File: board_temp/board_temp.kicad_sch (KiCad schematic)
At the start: 16 parts, among them J1 Conn_02x16_Odd_Even, J2 Battery input, J3 USB_C_Receptacle_PowerOnly_6P, SW1 SW_SP3T, U1 BQ24074RGT, U2 INA219AxDCN, U3 IP2721

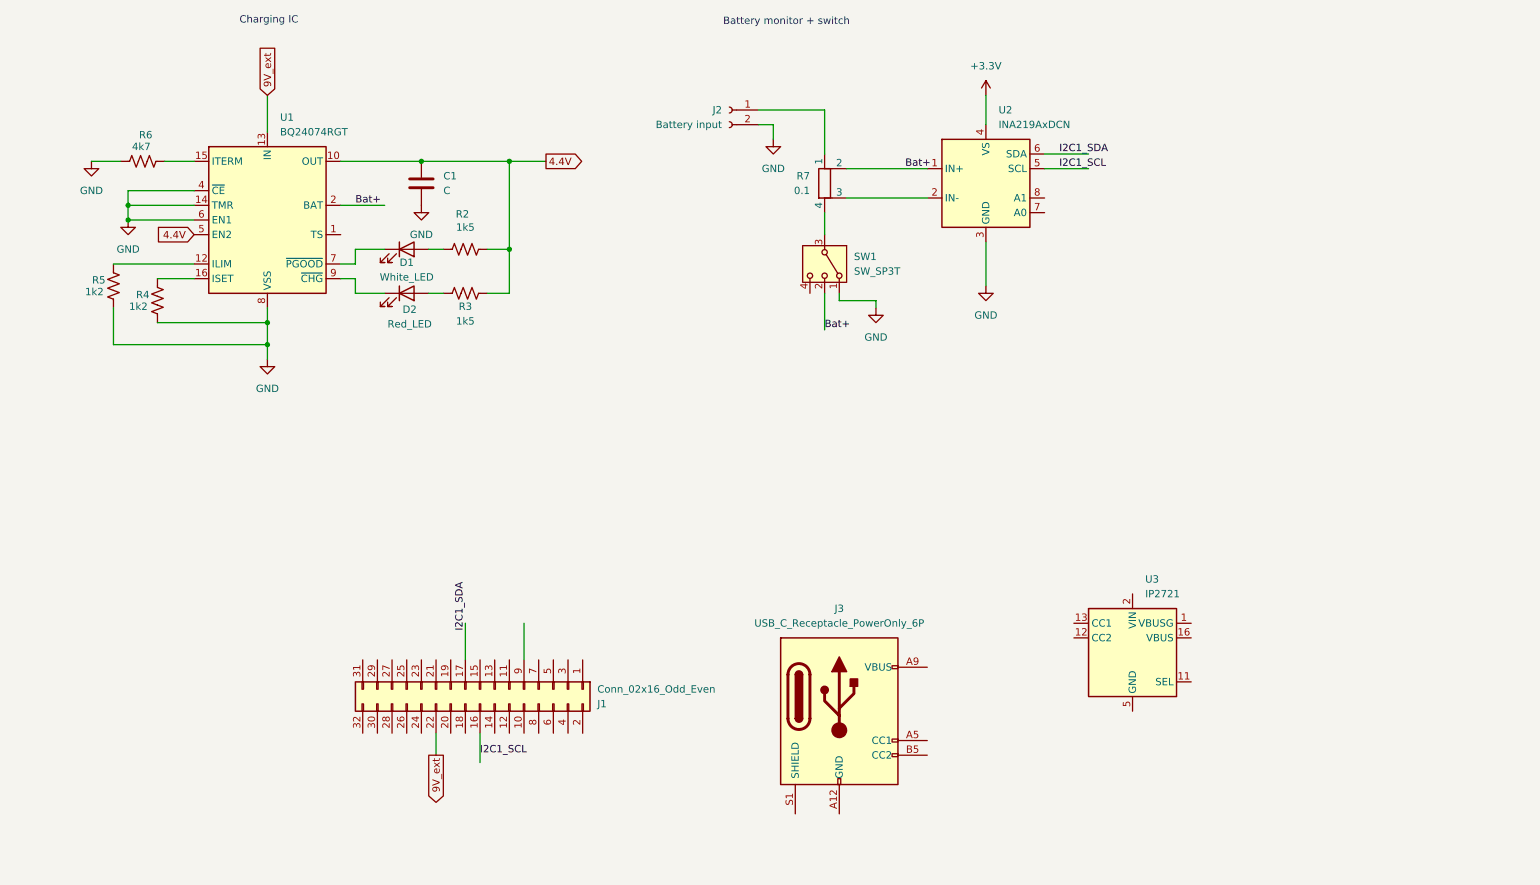
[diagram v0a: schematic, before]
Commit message: changed charging config
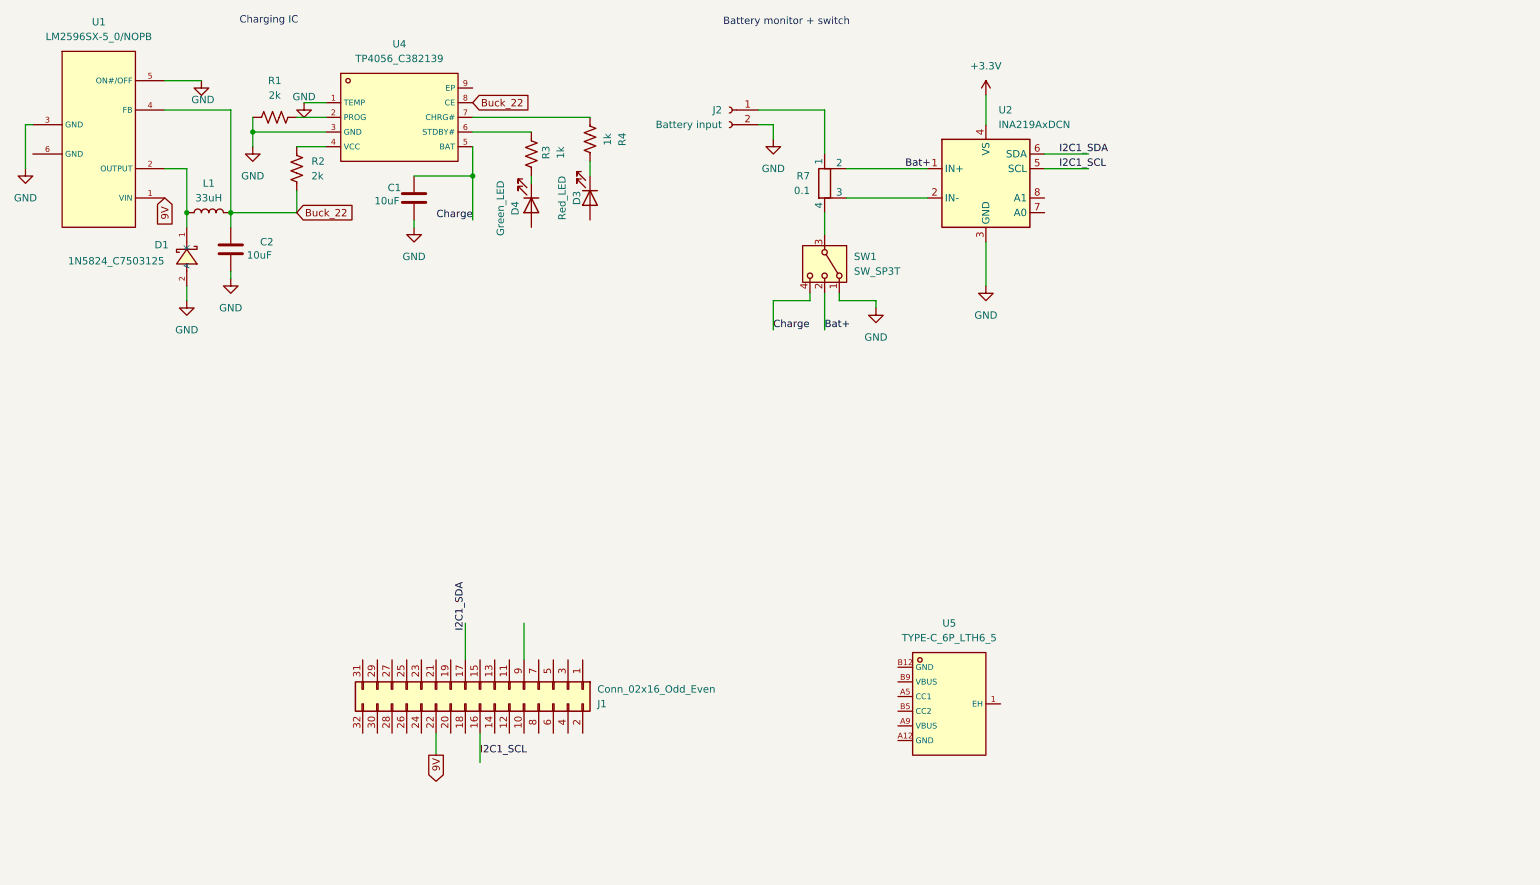
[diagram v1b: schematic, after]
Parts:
- removed D1: White_LED, symbol Device:LED
- removed D2: Red_LED, symbol Device:LED
- removed J3: USB_C_Receptacle_PowerOnly_6P, symbol Connector:USB_C_Receptacle_PowerOnly_6P
- removed R5: 1k2, symbol Device:R_US
- removed R6: 4k7, symbol Device:R_US
- removed U1: BQ24074RGT, Package_DFN_QFN:VQFN-16-1EP_3x3mm_P0.5mm_EP1.6x1.6mm, symbol Battery_Management:BQ24074RGT
- removed U3: IP2721, Package_SO:TSSOP-16_4.4x5mm_P0.65mm, symbol Interface_USB:IP2721
- added C2: 10uF, symbol Device:C
- added D1: 1N5824_C7503125, xxcustom_footprint:DO-27_BD5.3-L8.4-P12.40-D1.3-RD, symbol 1N5824_C7503125:1N5824_C7503125
- added D3: Red_LED, symbol Device:LED
- added D4: Green_LED, symbol Device:LED
- added L1: 33uH, symbol Device:L
- added R1: 2k, xxcustom_footprint:R0402, symbol Device:R_US
- added U1: LM2596SX-5_0/NOPB, xxcustom_footprint:TO-263-5_L10.2-W8.9-P1.70-TL, symbol LM2596SX-5_0/NOPB:LM2596SX-5_0/NOPB
- added U4: TP4056_C382139, xxcustom_footprint:ESOP-8_L4.9-W3.9-P1.27-LS6.0-BL-EP, symbol TP4056_C382139:TP4056_C382139
- added U5: TYPE-C_6P_LTH6_5, xxcustom_footprint:USB-TYPE-C-SMD_TYPE-C-6P-LTH6.5, symbol TYPE-C_6P_LTH6_5:TYPE-C_6P_LTH6_5
- C1: value C -> 10uF
- R2: value 1k5 -> 2k; footprint (none) -> xxcustom_footprint:R0402
- R3: value 1k5 -> 1k; footprint (none) -> xxcustom_footprint:R0402
- R4: value 1k2 -> 1k; footprint (none) -> xxcustom_footprint:R0402
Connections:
- net GND: now also C2.2, D1.2 (A), R1.1, U1.3 (GND), U1.5 (ON#/OFF), U4.1 (TEMP), U4.3 (GND); no longer R4.1
- net at R4.2: now also U4.7 (CHRG#)
- net Charge: now reaches SW1.4
- net Charge: now also C1.1, U4.5 (BAT)
- net at R3.1: now also U4.6 (STDBY#)
- net Buck_22: now reaches R2.1
- net Buck_22: now also C2.1, L1.2, U1.4 (FB), U4.8 (CE)
- removed net 4.4V: C1.1, R2.2, R3.2
- net 9V_ext renamed 9V
- net 9V: now also U1.1 (VIN)
- new net: D3.1 (K), R4.1
- new net: D1.1 (K), L1.1, U1.2 (OUTPUT)
- new net: D4.1 (K), R3.2
- new net: R1.2, U4.2 (PROG)
- new net: R2.2, U4.4 (VCC)

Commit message: reorganized some files
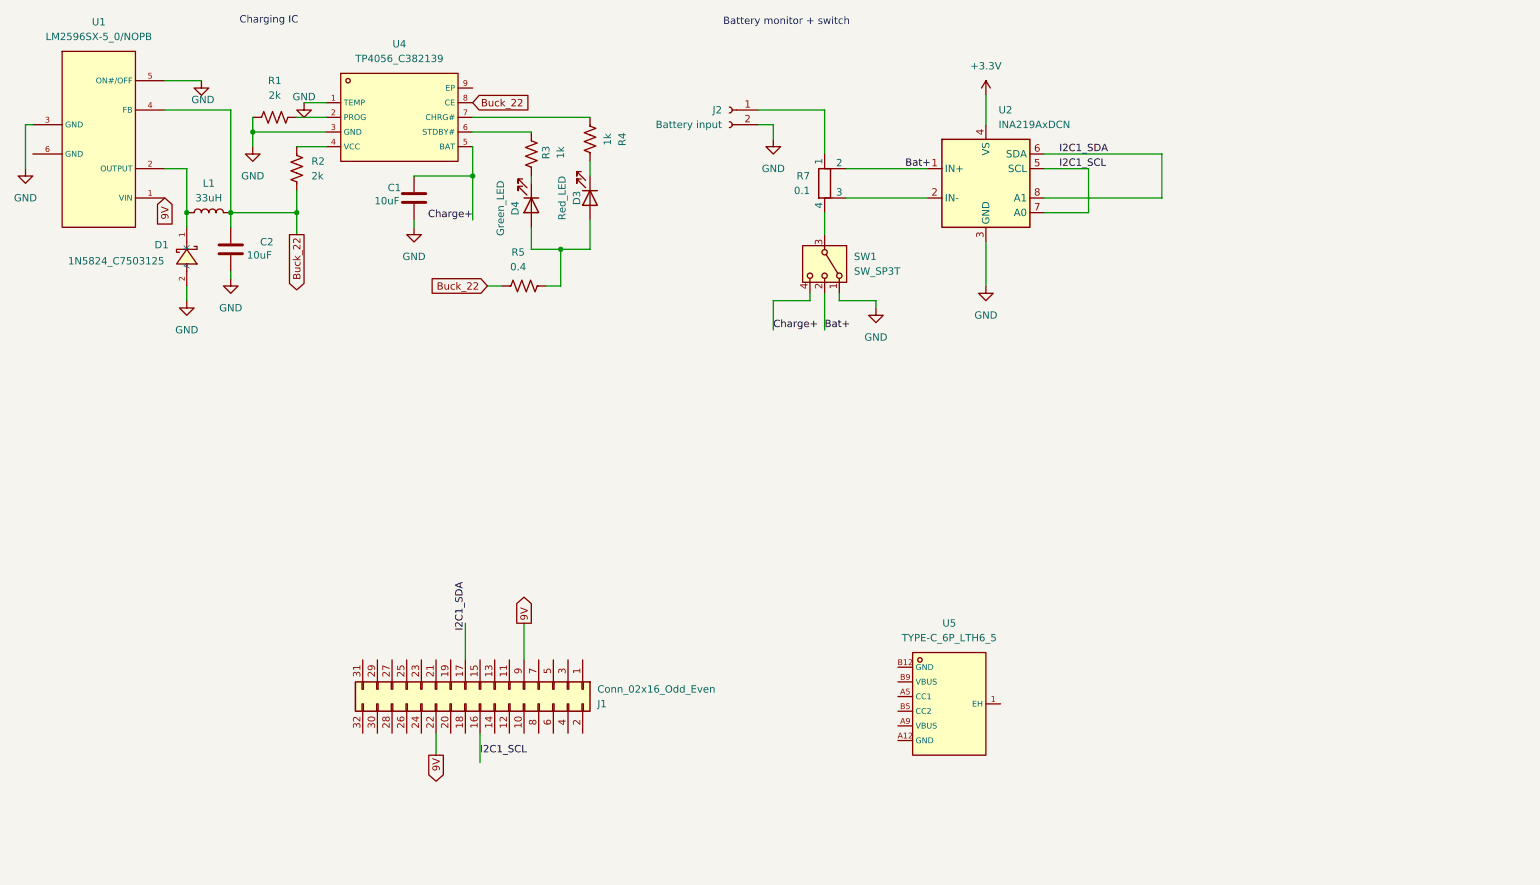
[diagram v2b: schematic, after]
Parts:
- added R5: 0.4, symbol Device:R_US
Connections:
- net 9V: now also J1.9 (Pin_9)
- net Buck_22: now also R5.1
- net I2C1_SCL: now also U2.7 (A0)
- net I2C1_SDA: now also U2.8 (A1)
- net at D3.2 (A): now also D4.2 (A), R5.2
- net Charge renamed Charge+
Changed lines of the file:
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@@
+	)
+	(junction
+		(at 106.68 58.42)
+		(diameter 0)
+		(color 0 0 0 0)
 	)
 	(junction
@@
 		(color 0 0 0 0)
 	)
+	(junction
+		(at 60.96 52.07)
+		(diameter 0)
+		(color 0 0 0 0)
+	)
 	(wire
 		(pts
@@
 	(wire
 		(pts
+			(xy 101.6 54.61) (xy 101.6 58.42)
+		)
+		(stroke
+			(width 0)
+			(type default)
+		)
+	)
+	(wire
+		(pts
 			(xy 101.6 46.99) (xy 101.6 45.72)
 		)
@@
 	(wire
 		(pts
+			(xy 101.6 58.42) (xy 106.68 58.42)
+		)
+		(stroke
+			(width 0)
+			(type default)
+		)
+	)
+	(wire
+		(pts
 			(xy 49.53 62.23) (xy 49.53 63.5)
 		)
@@
 	(wire
 		(pts
+			(xy 106.68 58.42) (xy 111.76 58.42)
+		)
+		(stroke
+			(width 0)
+			(type default)
+		)
+	)
+	(wire
+		(pts
 			(xy 190.5 44.45) (xy 198.12 44.45)
 		)
@@
 	(wire
 		(pts
+			(xy 93.98 64.77) (xy 96.52 64.77)
+		)
+		(stroke
+			(width 0)
+			(type default)
+		)
+	)
+	(wire
+		(pts
+			(xy 111.76 53.34) (xy 111.76 58.42)
+		)
+		(stroke
+			(width 0)
+			(type default)
+		)
+	)
+	(wire
+		(pts
 			(xy 111.76 45.72) (xy 111.76 43.18)
 		)
@@
 	(wire
 		(pts
+			(xy 190.5 52.07) (xy 198.12 52.07)
+		)
+		(stroke
+			(width 0)
+			(type default)
+		)
+	)
+	(wire
+		(pts
 			(xy 156.21 44.45) (xy 170.18 44.45)
 		)
@@
 	(wire
 		(pts
+			(xy 106.68 58.42) (xy 106.68 64.77)
+		)
+		(stroke
+			(width 0)
+			(type default)
+		)
+	)
+	(wire
+		(pts
 			(xy 143.51 36.83) (xy 143.51 39.37)
 		)
@@
 	(wire
 		(pts
+			(xy 60.96 52.07) (xy 60.96 55.88)
+		)
+		(stroke
+			(width 0)
+			(type default)
+		)
+	)
+	(wire
+		(pts
 			(xy 92.71 142.24) (xy 92.71 147.32)
 		)
@@
 	(wire
 		(pts
+			(xy 210.82 49.53) (xy 210.82 41.91)
+		)
+		(stroke
+			(width 0)
+			(type default)
+		)
+	)
+	(wire
+		(pts
 			(xy 152.4 52.07) (xy 152.4 55.88)
 		)
@@
 	(wire
 		(pts
-			(xy 190.5 41.91) (xy 198.12 41.91)
+			(xy 190.5 41.91) (xy 210.82 41.91)
 		)
 		(stroke
@@
 	(wire
 		(pts
+			(xy 198.12 52.07) (xy 198.12 44.45)
+		)
+		(stroke
+			(width 0)
+			(type default)
+		)
+	)
+	(wire
+		(pts
+			(xy 104.14 64.77) (xy 106.68 64.77)
+		)
+		(stroke
+			(width 0)
+			(type default)
+		)
+	)
+	(wire
+		(pts
 			(xy 49.53 34.29) (xy 49.53 52.07)
 		)
@@
 		(pts
 			(xy 38.1 44.45) (xy 41.91 44.45)
+		)
+		(stroke
+			(width 0)
+			(type default)
+		)
+	)
+	(wire
+		(pts
+			(xy 190.5 49.53) (xy 210.82 49.53)
 		)
 		(stroke
@@
 		)
 	)
-	(label "Charge"
+	(label "Charge+"
 		(at 143.51 72.39 0)
 		(effects
@@
 		)
 	)
-	(label "Charge"
+	(label "Charge+"
 		(at 91.44 53.34 180)
 		(effects
@@
 			)
 			(justify left bottom)
+		)
+	)
+	(global_label "Buck_22"
+		(shape output)
+		(at 60.96 55.88 270)
+		(fields_autoplaced yes)
+		(effects
+			(font
+				(size 1.27 1.27)
+			)
+			(justify right)
+		)
+		(property "Intersheetrefs" "${INTERSHEET_REFS}"
+			(at 60.96 66.7875 90)
+			(effects
+				(font
+					(size 1.27 1.27)
+				)
+				(justify right)
+				(hide yes)
+			)
+		)
+	)
+	(global_label "9V"
+		(shape output)
+		(at 100.33 123.19 90)
+		(fields_autoplaced yes)
+		(effects
+			(font
+				(size 1.27 1.27)
+			)
+			(justify left)
+		)
+		(property "Intersheetrefs" "${INTERSHEET_REFS}"
+			(at 100.33 117.9067 90)
+			(effects
+				(font
+					(size 1.27 1.27)
+				)
+				(justify left)
+				(hide yes)
+			)
 		)
 	)
@@
 	(global_label "Buck_22"
 		(shape input)
-		(at 60.96 52.07 0)
+		(at 93.98 64.77 180)
 		(fields_autoplaced yes)
 		(effects
@@
 				(size 1.27 1.27)
 			)
-			(justify left)
+			(justify right)
 		)
 		(property "Intersheetrefs" "${INTERSHEET_REFS}"
-			(at 71.8675 52.07 0)
-			(effects
-				(font
-					(size 1.27 1.27)
-				)
-				(justify left)
+			(at 83.0725 64.77 0)
+			(effects
+				(font
+					(size 1.27 1.27)
+				)
+				(justify right)
 				(hide yes)
 			)
@@
 					(unit 1)
 				)
+			)
+		)
+	)
+	(symbol
+		(lib_id "Device:R_US")
+		(at 100.33 64.77 90)
+		(unit 1)
+		(exclude_from_sim no)
+		(in_bom yes)
+		(on_board yes)
+		(dnp no)
+		(property "Reference" "R5"
+			(at 99.314 58.928 90)
+			(effects
+				(font
+					(size 1.27 1.27)
+				)
+			)
+		)
+		(property "Value" "0.4"
+			(at 99.314 61.468 90)
+			(effects
+				(font
+					(size 1.27 1.27)
+				)
+			)
+		)
+		(property "Footprint" ""
+			(at 100.584 63.754 90)
+			(effects
+				(font
+					(size 1.27 1.27)
+				)
+				(hide yes)
+			)
+		)
+		(property "Datasheet" "~"
+			(at 100.33 64.77 0)
+			(effects
+				(font
+					(size 1.27 1.27)
+				)
+				(hide yes)
+			)
+		)
+		(property "Description" "Resistor, US symbol"
+			(at 100.33 64.77 0)
+			(effects
+				(font
+					(size 1.27 1.27)
+				)
+				(hide yes)
+			)
+		)
+		(pin "2"
+		)
+		(pin "1"
+		)
+		(instances
+			(project ""
+				(path "/0d835796-a84c-45a9-a747-a1ce772a6e73"
+					(reference "R5")
+					(unit 1)
+				)

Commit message: added USB PD
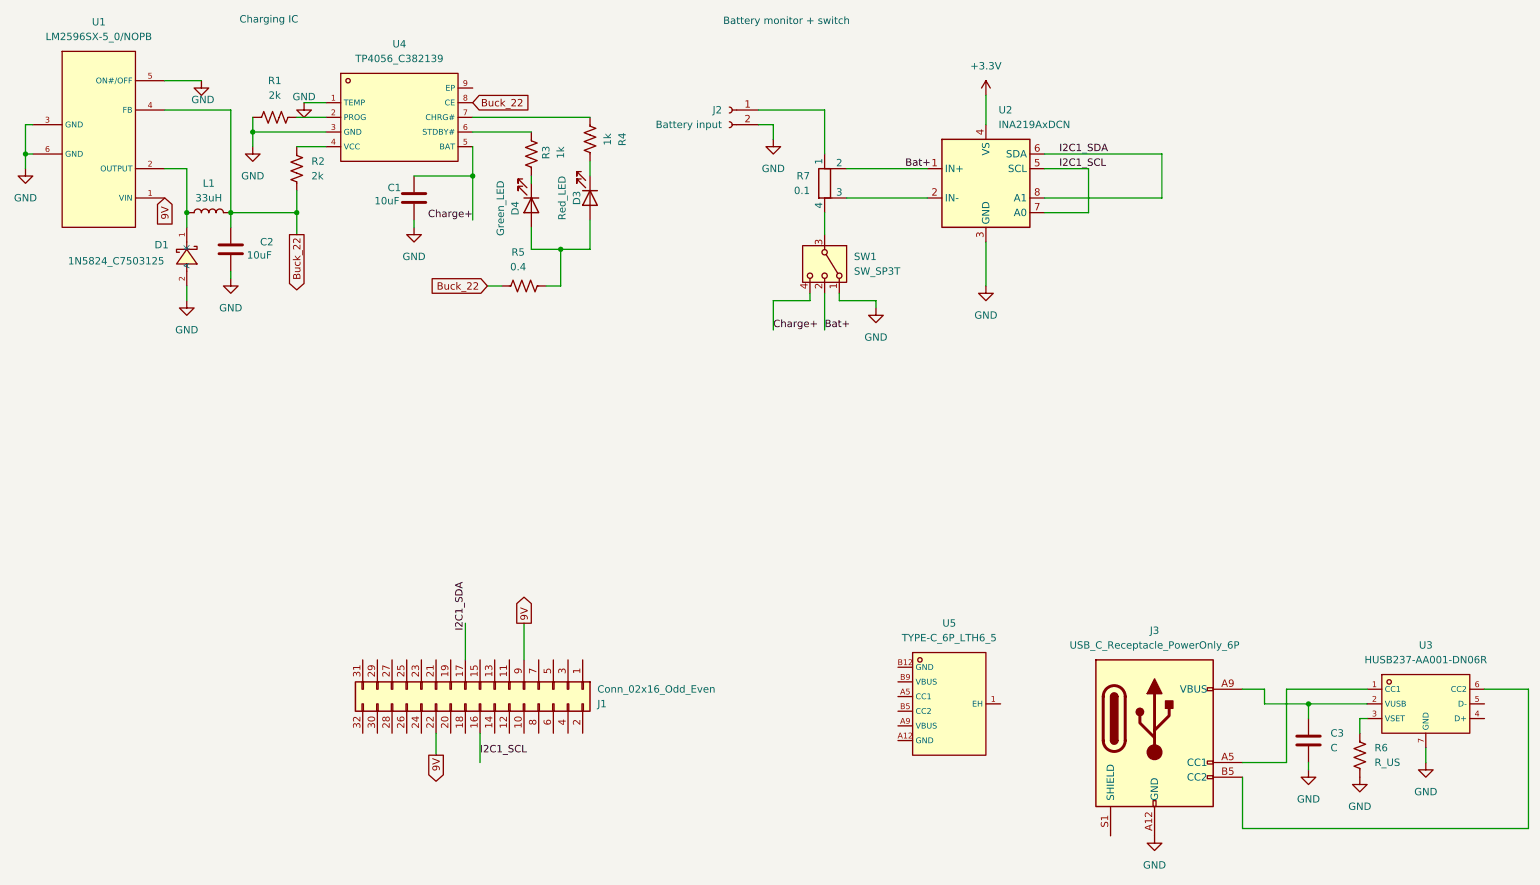
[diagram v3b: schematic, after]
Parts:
- added C3: C, symbol Device:C
- added J3: USB_C_Receptacle_PowerOnly_6P, symbol Connector:USB_C_Receptacle_PowerOnly_6P
- added R6: R_US, symbol Device:R_US
- added U3: HUSB237-AA001-DN06R, xxcustom_footprint:TDFN-6_L2.0-W2.0-P0.65-TL-EP, symbol HUSB237-AA001-DN06R:HUSB237-AA001-DN06R
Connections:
- net GND: now also U1.6 (GND), C3.2, J3.A12 (GND), J3.B12 (GND), R6.2, U3.7 (GND)
- new net: C3.1, J3.A9 (VBUS), J3.B9 (VBUS), U3.2 (VUSB)
- new net: J3.A5 (CC1), U3.1 (CC1)
- new net: J3.B5 (CC2), U3.6 (CC2)
- new net: R6.1, U3.3 (VSET)
